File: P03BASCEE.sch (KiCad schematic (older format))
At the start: 13 parts, among them U1 24LC1025, U2 24LC1025, U3 DS1337_PD, U4 ATMEGA328P-AU, Y1 Crystal, Y2 Crystal

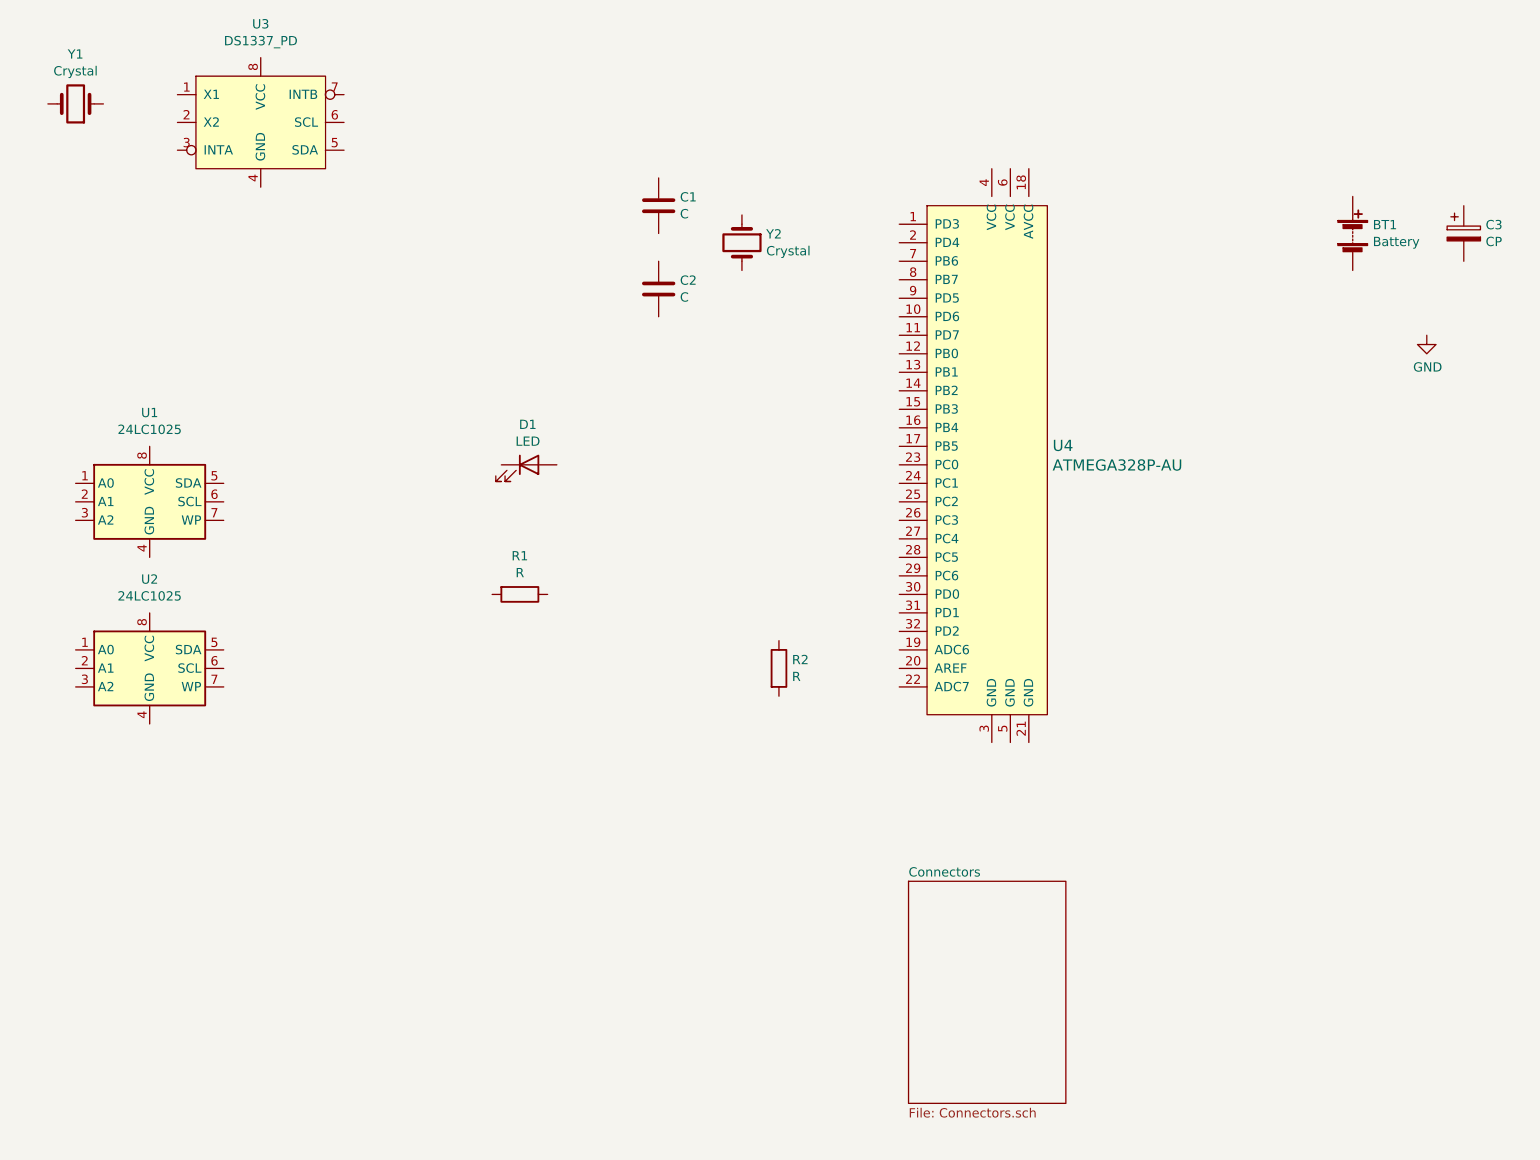
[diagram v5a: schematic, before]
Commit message: Todos os valores e footprints adicionados
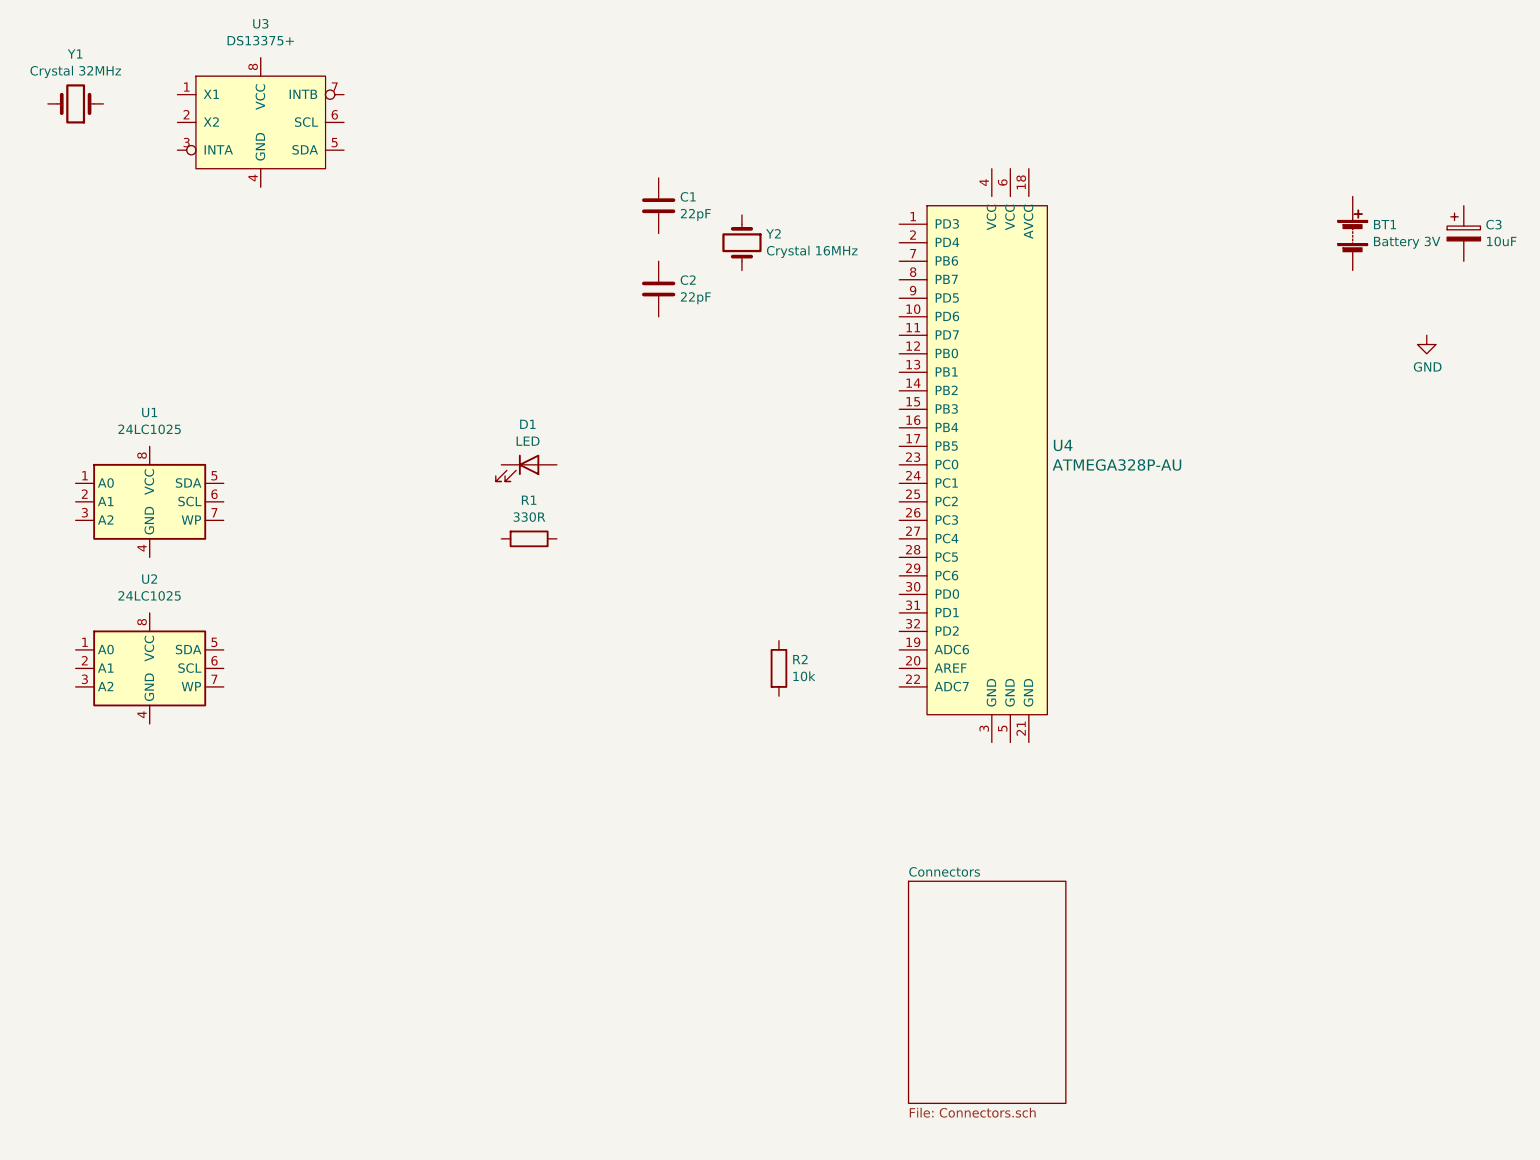
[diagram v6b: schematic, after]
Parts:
- BT1: value Battery -> Battery 3V; footprint (none) -> Connector_JST:JST_PH_B2B-PH-K_1x02_P2.00mm_Vertical
- C1, C2: value C -> 22pF; footprint (none) -> Capacitor_SMD:C_0805_2012Metric
- C3: value CP -> 10uF; footprint (none) -> Capacitor_SMD:C_0805_2012Metric
- D1: footprint (none) -> LED_SMD:LED_0805_2012Metric
- R1: value R -> 330R; footprint (none) -> Resistor_SMD:R_0805_2012Metric
- R2: value R -> 10k; footprint (none) -> Resistor_SMD:R_0805_2012Metric
- U1, U2: footprint (none) -> Package_SO:SO-8_5.3x6.2mm_P1.27mm
- U3: value DS1337_PD -> DS13375+; footprint (none) -> Package_SO:SO-8_5.3x6.2mm_P1.27mm
- Y1: value Crystal -> Crystal 32MHz; footprint (none) -> Crystal:Crystal_SMD_MicroCrystal_CC7V-T1A-2Pin_3.2x1.5mm
- Y2: value Crystal -> Crystal 16MHz; footprint (none) -> Crystal:Crystal_SMD_5032-2Pin_5.0x3.2mm_HandSoldering
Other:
- moved on the sheet: R1
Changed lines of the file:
@@
 P 8300 2550
 F 0 "BT1" H 8408 2596 50  0000 L CNN
-F 1 "Battery" H 8408 2505 50  0000 L CNN
-F 2 "" V 8300 2610 50  0001 C CNN
+F 1 "Battery 3V" H 8408 2505 50  0000 L CNN
+F 2 "Connector_JST:JST_PH_B2B-PH-K_1x02_P2.00mm_Vertical" V 8300 2610 50  0001 C CNN
 F 3 "~" V 8300 2610 50  0001 C CNN
 	1    8300 2550
@@
 P 8900 2550
 F 0 "C3" H 9018 2596 50  0000 L CNN
-F 1 "CP" H 9018 2505 50  0000 L CNN
-F 2 "" H 8938 2400 50  0001 C CNN
+F 1 "10uF" H 9018 2505 50  0000 L CNN
+F 2 "Capacitor_SMD:C_0805_2012Metric" H 8938 2400 50  0001 C CNN
 F 3 "~" H 8900 2550 50  0001 C CNN
 	1    8900 2550
@@
 P 4550 2850
 F 0 "C2" H 4665 2896 50  0000 L CNN
-F 1 "C" H 4665 2805 50  0000 L CNN
-F 2 "" H 4588 2700 50  0001 C CNN
+F 1 "22pF" H 4665 2805 50  0000 L CNN
+F 2 "Capacitor_SMD:C_0805_2012Metric" H 4588 2700 50  0001 C CNN
 F 3 "~" H 4550 2850 50  0001 C CNN
 	1    4550 2850
@@
 F 0 "D1" H 3843 4017 50  0000 C CNN
 F 1 "LED" H 3843 3926 50  0000 C CNN
-F 2 "" H 3850 3800 50  0001 C CNN
+F 2 "LED_SMD:LED_0805_2012Metric" H 3850 3800 50  0001 C CNN
 F 3 "~" H 3850 3800 50  0001 C CNN
 	1    3850 3800
@@
 P 4550 2400
 F 0 "C1" H 4665 2446 50  0000 L CNN
-F 1 "C" H 4665 2355 50  0000 L CNN
-F 2 "" H 4588 2250 50  0001 C CNN
+F 1 "22pF" H 4665 2355 50  0000 L CNN
+F 2 "Capacitor_SMD:C_0805_2012Metric" H 4588 2250 50  0001 C CNN
 F 3 "~" H 4550 2400 50  0001 C CNN
 	1    4550 2400
@@
 L Device:R R1
 U 1 1 5F033AAA
-P 3800 4500
-F 0 "R1" V 3593 4500 50  0000 C CNN
-F 1 "R" V 3684 4500 50  0000 C CNN
-F 2 "" V 3730 4500 50  0001 C CNN
-F 3 "~" H 3800 4500 50  0001 C CNN
-	1    3800 4500
+P 3850 4200
+F 0 "R1" V 3643 4200 50  0000 C CNN
+F 1 "330R" V 3734 4200 50  0000 C CNN
+F 2 "Resistor_SMD:R_0805_2012Metric" V 3780 4200 50  0001 C CNN
+F 3 "~" H 3850 4200 50  0001 C CNN
+	1    3850 4200
 	0    1    1    0
 $EndComp
@@
 P 5200 4900
 F 0 "R2" H 5270 4946 50  0000 L CNN
-F 1 "R" H 5270 4855 50  0000 L CNN
-F 2 "" V 5130 4900 50  0001 C CNN
+F 1 "10k" H 5270 4855 50  0000 L CNN
+F 2 "Resistor_SMD:R_0805_2012Metric" V 5130 4900 50  0001 C CNN
 F 3 "~" H 5200 4900 50  0001 C CNN
 	1    5200 4900
@@
 F 0 "U1" H 1800 4481 50  0000 C CNN
 F 1 "24LC1025" H 1800 4390 50  0000 C CNN
-F 2 "" H 1800 4000 50  0001 C CNN
+F 2 "Package_SO:SO-8_5.3x6.2mm_P1.27mm" H 1800 4000 50  0001 C CNN
 F 3 "http://ww1.microchip.com/downloads/en/DeviceDoc/21941B.pdf" H 1800 4000 50  0001 C CNN
 	1    1800 4000
@@
 P 2400 1950
 F 0 "U3" H 2400 2481 50  0000 C CNN
-F 1 "DS1337_PD" H 2400 2390 50  0000 C CNN
-F 2 "" H 2400 2350 50  0001 C CNN
+F 1 "DS13375+" H 2400 2390 50  0000 C CNN
+F 2 "Package_SO:SO-8_5.3x6.2mm_P1.27mm" H 2400 2350 50  0001 C CNN
 F 3 "https://datasheets.maximintegrated.com/en/ds/DS1337-DS1337C.pdf" H 2400 2350 50  0001 C CNN
 	1    2400 1950
@@
 P 5000 2600
 F 0 "Y2" V 4954 2731 50  0000 L CNN
-F 1 "Crystal" V 5045 2731 50  0000 L CNN
-F 2 "" H 5000 2600 50  0001 C CNN
+F 1 "Crystal 16MHz" V 5045 2731 50  0000 L CNN
+F 2 "Crystal:Crystal_SMD_5032-2Pin_5.0x3.2mm_HandSoldering" H 5000 2600 50  0001 C CNN
 F 3 "~" H 5000 2600 50  0001 C CNN
 	1    5000 2600
@@
 P 1400 1850
 F 0 "Y1" H 1400 1582 50  0000 C CNN
-F 1 "Crystal" H 1400 1673 50  0000 C CNN
-F 2 "" H 1400 1850 50  0001 C CNN
+F 1 "Crystal 32MHz" H 1400 1673 50  0000 C CNN
+F 2 "Crystal:Crystal_SMD_MicroCrystal_CC7V-T1A-2Pin_3.2x1.5mm" H 1400 1850 50  0001 C CNN
 F 3 "~" H 1400 1850 50  0001 C CNN
 	1    1400 1850
@@
 F 0 "U2" H 1800 5381 50  0000 C CNN
 F 1 "24LC1025" H 1800 5290 50  0000 C CNN
-F 2 "" H 1800 4900 50  0001 C CNN
+F 2 "Package_SO:SO-8_5.3x6.2mm_P1.27mm" H 1800 4900 50  0001 C CNN
 F 3 "http://ww1.microchip.com/downloads/en/DeviceDoc/21941B.pdf" H 1800 4900 50  0001 C CNN
 	1    1800 4900

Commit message: Ligação dos conectores
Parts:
- BT1: footprint Connector_JST:JST_PH_B2B-PH-K_1x02_P2.00mm_Vertical -> Connector_JST:JST_PH_S2B-PH-K_1x02_P2.00mm_Horizontal
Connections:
- net GND: now also U4.21 (GND), U4.3 (GND), U4.5 (GND)
- net D3: now reaches U4.1 (PD3)
- net D6: now reaches U4.10 (PD6)
- net D7: now reaches U4.11 (PD7)
- net D8: now reaches U4.12 (PB0)
- net MOSI: now reaches U4.15 (PB3)
- net MISO: now reaches U4.16 (PB4)
- net SCK: now reaches U4.17 (PB5)
- net VCC: now reaches U4.18 (AVCC)
- net VCC: now also U4.4 (VCC), U4.6 (VCC)
- net D4: now reaches U4.2 (PD4)
- net SDA: now reaches U4.27 (PC4)
- net RESET: now reaches U4.29 (PC6)
- net RX: now reaches U4.30 (PD0)
- net TX: now reaches U4.31 (PD1)
- net D2: now reaches U4.32 (PD2)
- net D5: now reaches U4.9 (PD5)
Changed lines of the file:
@@
 F 0 "BT1" H 8408 2596 50  0000 L CNN
 F 1 "Battery 3V" H 8408 2505 50  0000 L CNN
-F 2 "Connector_JST:JST_PH_B2B-PH-K_1x02_P2.00mm_Vertical" V 8300 2610 50  0001 C CNN
+F 2 "Connector_JST:JST_PH_S2B-PH-K_1x02_P2.00mm_Horizontal" V 8300 2610 50  0001 C CNN
 F 3 "~" V 8300 2610 50  0001 C CNN
 	1    8300 2550
@@
 	1    0    0    -1
 $EndComp
+$Comp
+L DS1337:DS1337_PD U3
+U 1 1 5F04ABB9
+P 2400 1950
+F 0 "U3" H 2400 2481 50  0000 C CNN
+F 1 "DS13375+" H 2400 2390 50  0000 C CNN
+F 2 "Package_SO:SO-8_5.3x6.2mm_P1.27mm" H 2400 2350 50  0001 C CNN
+F 3 "https://datasheets.maximintegrated.com/en/ds/DS1337-DS1337C.pdf" H 2400 2350 50  0001 C CNN
+	1    2400 1950
+	1    0    0    -1
+$EndComp
+$Comp
+L Device:Crystal Y2
+U 1 1 5F04BC1B
+P 5000 2600
+F 0 "Y2" V 4954 2731 50  0000 L CNN
+F 1 "Crystal 16MHz" V 5045 2731 50  0000 L CNN
+F 2 "Crystal:Crystal_SMD_5032-2Pin_5.0x3.2mm_HandSoldering" H 5000 2600 50  0001 C CNN
+F 3 "~" H 5000 2600 50  0001 C CNN
+	1    5000 2600
+	0    1    1    0
+$EndComp
+$Comp
+L Device:Crystal Y1
+U 1 1 5F04CD00
+P 1400 1850
+F 0 "Y1" H 1400 1582 50  0000 C CNN
+F 1 "Crystal 32MHz" H 1400 1673 50  0000 C CNN
+F 2 "Crystal:Crystal_SMD_MicroCrystal_CC7V-T1A-2Pin_3.2x1.5mm" H 1400 1850 50  0001 C CNN
+F 3 "~" H 1400 1850 50  0001 C CNN
+	1    1400 1850
+	-1   0    0    1
+$EndComp
+$Comp
+L Memory_EEPROM:24LC1025 U2
+U 1 1 5F05520E
+P 1800 4900
+F 0 "U2" H 1800 5381 50  0000 C CNN
+F 1 "24LC1025" H 1800 5290 50  0000 C CNN
+F 2 "Package_SO:SO-8_5.3x6.2mm_P1.27mm" H 1800 4900 50  0001 C CNN
+F 3 "http://ww1.microchip.com/downloads/en/DeviceDoc/21941B.pdf" H 1800 4900 50  0001 C CNN
+	1    1800 4900
+	1    0    0    -1
+$EndComp
+$Comp
+L power:GND #PWR01
+U 1 1 5F0655B3
+P 8700 3100
+F 0 "#PWR01" H 8700 2850 50  0001 C CNN
+F 1 "GND" H 8705 2927 50  0000 C CNN
+F 2 "" H 8700 3100 50  0001 C CNN
+F 3 "" H 8700 3100 50  0001 C CNN
+	1    8700 3100
+	1    0    0    -1
+$EndComp
+Text Label 5300 6100 2    50   ~ 0
+MISO
+Text Label 5850 3600 2    50   ~ 0
+MISO
+Wire Wire Line
+	5300 6100 5500 6100
+Text Label 5300 6200 2    50   ~ 0
+SCK
+Text Label 5300 6300 2    50   ~ 0
+RESET
+Text Label 5300 7000 2    50   ~ 0
+VCC
+Text Label 5300 6400 2    50   ~ 0
+MOSI
+Text Label 5300 7100 2    50   ~ 0
+GND
+Wire Wire Line
+	5300 6400 5500 6400
+Wire Wire Line
+	5300 6300 5500 6300
+Wire Wire Line
+	5500 6200 5300 6200
+Wire Wire Line
+	5300 7100 5350 7100
+Wire Wire Line
+	5500 7000 5300 7000
+Text Label 5850 3500 2    50   ~ 0
+MOSI
+Text Label 5850 3700 2    50   ~ 0
+SCK
+Text Label 5850 4400 2    50   ~ 0
+RESET
+Text Label 6350 1950 2    50   ~ 0
+VCC
+Wire Wire Line
+	6350 1950 6450 1950
+Wire Wire Line
+	6450 1950 6450 2100
+Wire Wire Line
+	6350 2200 6350 2100
+Wire Wire Line
+	6350 2100 6450 2100
+Connection ~ 6450 2100
+Wire Wire Line
+	6450 2100 6450 2200
+Wire Wire Line
+	6550 2200 6550 2100
+Wire Wire Line
+	6550 2100 6450 2100
+Text Label 6450 5500 2    50   ~ 0
+GND
+Wire Wire Line
+	6350 5300 6350 5400
+Wire Wire Line
+	6350 5400 6450 5400
+Wire Wire Line
+	6450 5400 6450 5500
+Wire Wire Line
+	6450 5300 6450 5400
+Connection ~ 6450 5400
+Wire Wire Line
+	6550 5300 6550 5400
+Wire Wire Line
+	6550 5400 6450 5400
+$Comp
+L power:GND #PWR?
+U 1 1 5F080AFD
+P 6450 5500
+F 0 "#PWR?" H 6450 5250 50  0001 C CNN
+F 1 "GND" H 6455 5327 50  0000 C CNN
+F 2 "" H 6450 5500 50  0001 C CNN
+F 3 "" H 6450 5500 50  0001 C CNN
+	1    6450 5500
+	1    0    0    -1
+$EndComp
+$Comp
+L power:GND #PWR?
+U 1 1 5F0812AD
+P 5350 7100
+F 0 "#PWR?" H 5350 6850 50  0001 C CNN
+F 1 "GND" H 5355 6927 50  0000 C CNN
+F 2 "" H 5350 7100 50  0001 C CNN
+F 3 "" H 5350 7100 50  0001 C CNN
+	1    5350 7100
+	1    0    0    -1
+$EndComp
+Connection ~ 5350 7100
+Wire Wire Line
+	5350 7100 5500 7100
 $Sheet
-S 5900 6050 850  1200
+S 5500 6000 850  1200
 U 5F03AF31
 F0 "Connectors" 50
 F1 "Connectors.sch" 50
+F2 "MISO" O L 5500 6100 50
+F3 "SCK" B L 5500 6200 50
+F4 "RESET" O L 5500 6300 50
+F5 "VCC" I L 5500 7000 50
+F6 "MOSI" I L 5500 6400 50
+F7 "GND" I L 5500 7100 50
+F8 "RX" I L 5500 6550 50
+F9 "TX" O L 5500 6650 50
+F10 "SDA" B L 5500 6750 50
+F11 "D2" B R 6350 6500 50
+F12 "D3" B R 6350 6600 50
+F13 "D4" B R 6350 6700 50
+F14 "D5" B R 6350 6800 50
+F15 "D6" B R 6350 6900 50
+F16 "D7" B R 6350 7000 50
+F17 "D8" B R 6350 7100 50
 $EndSheet
+Wire Wire Line
+	6350 6500 6500 6500
+Wire Wire Line
+	6350 6600 6500 6600
+Wire Wire Line
+	6350 6700 6500 6700
+Wire Wire Line
+	6350 6800 6500 6800
+Wire Wire Line
+	6350 6900 6500 6900
+Wire Wire Line
+	6350 7100 6500 7100
+Wire Wire Line
+	5500 6550 5300 6550
+Wire Wire Line
+	5300 6650 5500 6650
+Wire Wire Line
+	5500 6750 5300 6750
+Text Label 5300 6550 2    50   ~ 0
+RX
+Text Label 5300 6650 2    50   ~ 0
+TX
+Text Label 5300 6750 2    50   ~ 0
+SDA
+Text Label 6500 6500 0    50   ~ 0
+D2
+Text Label 6500 6600 0    50   ~ 0
+D3
+Text Label 6500 6700 0    50   ~ 0
+D4
+Text Label 6500 6800 0    50   ~ 0
+D5
+Text Label 6500 6900 0    50   ~ 0
+D6
+Wire Wire Line
+	6350 7000 6500 7000
+Text Label 6500 7000 0    50   ~ 0
+D7
+Text Label 6500 7100 0    50   ~ 0
+D8
 $Comp
 L dk_Embedded-Microcontrollers:ATMEGA328P-AU U4
@@
 	1    0    0    -1
 $EndComp
-$Comp
-L DS1337:DS1337_PD U3
-U 1 1 5F04ABB9
-P 2400 1950
-F 0 "U3" H 2400 2481 50  0000 C CNN
-F 1 "DS13375+" H 2400 2390 50  0000 C CNN
-F 2 "Package_SO:SO-8_5.3x6.2mm_P1.27mm" H 2400 2350 50  0001 C CNN
-F 3 "https://datasheets.maximintegrated.com/en/ds/DS1337-DS1337C.pdf" H 2400 2350 50  0001 C CNN
-	1    2400 1950
-	1    0    0    -1
-$EndComp
-$Comp
-L Device:Crystal Y2
-U 1 1 5F04BC1B
-P 5000 2600
-F 0 "Y2" V 4954 2731 50  0000 L CNN
-F 1 "Crystal 16MHz" V 5045 2731 50  0000 L CNN
-F 2 "Crystal:Crystal_SMD_5032-2Pin_5.0x3.2mm_HandSoldering" H 5000 2600 50  0001 C CNN
-F 3 "~" H 5000 2600 50  0001 C CNN
-	1    5000 2600
-	0    1    1    0
-$EndComp
-$Comp
-L Device:Crystal Y1
-U 1 1 5F04CD00
-P 1400 1850
-F 0 "Y1" H 1400 1582 50  0000 C CNN
-F 1 "Crystal 32MHz" H 1400 1673 50  0000 C CNN
-F 2 "Crystal:Crystal_SMD_MicroCrystal_CC7V-T1A-2Pin_3.2x1.5mm" H 1400 1850 50  0001 C CNN
-F 3 "~" H 1400 1850 50  0001 C CNN
-	1    1400 1850
-	-1   0    0    1
-$EndComp
-$Comp
-L Memory_EEPROM:24LC1025 U2
-U 1 1 5F05520E
-P 1800 4900
-F 0 "U2" H 1800 5381 50  0000 C CNN
-F 1 "24LC1025" H 1800 5290 50  0000 C CNN
-F 2 "Package_SO:SO-8_5.3x6.2mm_P1.27mm" H 1800 4900 50  0001 C CNN
-F 3 "http://ww1.microchip.com/downloads/en/DeviceDoc/21941B.pdf" H 1800 4900 50  0001 C CNN
-	1    1800 4900
-	1    0    0    -1
-$EndComp
-$Comp
-L power:GND #PWR01
-U 1 1 5F0655B3
-P 8700 3100
-F 0 "#PWR01" H 8700 2850 50  0001 C CNN
-F 1 "GND" H 8705 2927 50  0000 C CNN
-F 2 "" H 8700 3100 50  0001 C CNN
-F 3 "" H 8700 3100 50  0001 C CNN
-	1    8700 3100
-	1    0    0    -1
-$EndComp
+Text Label 5850 2500 2    50   ~ 0
+D3
+Text Label 5850 2600 2    50   ~ 0
+D4
+Text Label 5850 2900 2    50   ~ 0
+D5
+Text Label 5850 3000 2    50   ~ 0
+D6
+Text Label 5850 3100 2    50   ~ 0
+D7
+Text Label 5850 3200 2    50   ~ 0
+D8
+Text Label 5850 4200 2    50   ~ 0
+SDA
+Text Label 5850 4500 2    50   ~ 0
+RX
+Text Label 5850 4600 2    50   ~ 0
+TX
+Text Label 5850 4700 2    50   ~ 0
+D2
 $EndSCHEMATC

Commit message: Feitas ligações entre componentes
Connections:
- net GND: now also BT1.2 (-), C1.2, C2.2, C3.2, D1.1 (K), U1.4 (GND), U1.7 (WP), U2.4 (GND), U2.7 (WP), U3.4 (GND)
- net RESET: now also R2.1
- net SCK: now also U1.6 (SCL), U2.6 (SCL), U3.6 (SCL), U4.28 (PC5); no longer U4.17 (PB5)
- net SDA: now also U1.5 (SDA), U2.5 (SDA), U3.5 (SDA)
- net VCC: now also BT1.1 (+), C3.1, R2.2, U1.3 (A2), U1.8 (VCC), U2.3 (A2), U2.8 (VCC), U3.3 (INTA), U3.8 (VCC), U4.20 (AREF)
- net at C2.1: now also U4.8 (PB7), Y2.2
- net at D1.2 (A): now also R1.2
- net at C1.1: now also U4.7 (PB6), Y2.1
- net at R1.1: now also U4.17 (PB5)
- net ADSS1: now reaches U1.1 (A0)
- net ADSS1: now also U2.1 (A0), U4.23 (PC0)
- net ADSS2: now reaches U1.2 (A1)
- net ADSS2: now also U2.2 (A1), U4.24 (PC1)
- net at U3.1 (X1): now also Y1.2
- net at U3.2 (X2): now also Y1.1
- no-connect marks 0 -> 7
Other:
- moved on the sheet: C1, C2, D1, R1, R2, U1, U2, U3, Y1, Y2
